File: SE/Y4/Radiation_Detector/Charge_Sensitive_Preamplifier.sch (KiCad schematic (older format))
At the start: 7 parts, among them U1 OP179GRT

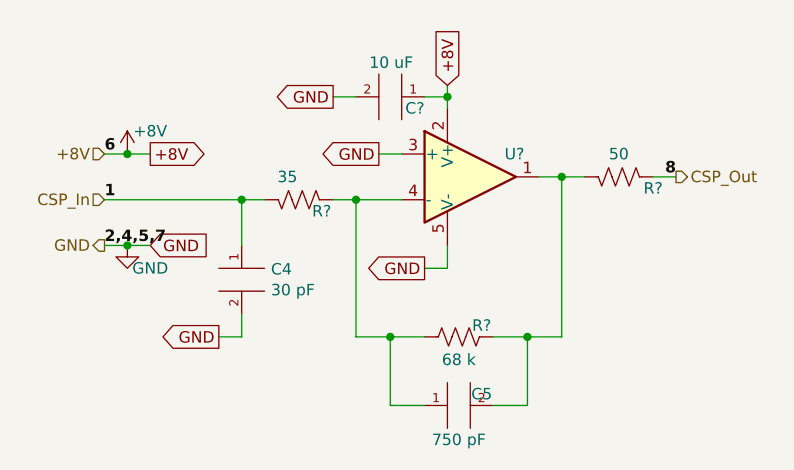
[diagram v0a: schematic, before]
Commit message: SiPM schematic symbol modified
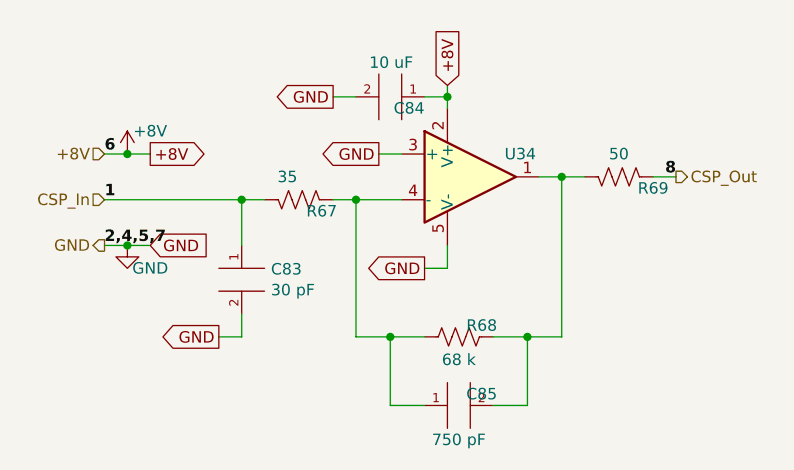
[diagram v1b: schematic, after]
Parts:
- gave numbers to parts that had none: 1
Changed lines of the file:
@@
 $Descr A4 11693 8268
 encoding utf-8
-Sheet 17 33
+Sheet 3 33
 Title ""
 Date ""
@@
 AR Path="/5EC116B0/5EBD2C07/5ED82FF2" Ref="#PWR061"  Part="1"
 AR Path="/5EC11F15/5EBD2C07/5ED82FF2" Ref="#PWR089"  Part="1"
-AR Path="/5EEC0C1C/5EBD2C07/5ED82FF2" Ref="#PWR?"  Part="1"
-AR Path="/5EEC180C/5EBD2C07/5ED82FF2" Ref="#PWR?"  Part="1"
-AR Path="/5EEC25A3/5EBD2C07/5ED82FF2" Ref="#PWR?"  Part="1"
-F 0 "#PWR?" H 1100 1900 50  0001 C CNN
+AR Path="/5EEC0C1C/5EBD2C07/5ED82FF2" Ref="#PWR0124"  Part="1"
+AR Path="/5EEC180C/5EBD2C07/5ED82FF2" Ref="#PWR0131"  Part="1"
+AR Path="/5EEC25A3/5EBD2C07/5ED82FF2" Ref="#PWR0138"  Part="1"
+F 0 "#PWR0138" H 1100 1900 50  0001 C CNN
 F 1 "+8V" H 1200 2150 50  0000 C CNN
 F 2 "" H 1100 2050 50  0001 C CNN
@@
 AR Path="/5EC116B0/5EBD2C07/5ED8301D" Ref="#PWR062"  Part="1"
 AR Path="/5EC11F15/5EBD2C07/5ED8301D" Ref="#PWR090"  Part="1"
-AR Path="/5EEC0C1C/5EBD2C07/5ED8301D" Ref="#PWR?"  Part="1"
-AR Path="/5EEC180C/5EBD2C07/5ED8301D" Ref="#PWR?"  Part="1"
-AR Path="/5EEC25A3/5EBD2C07/5ED8301D" Ref="#PWR?"  Part="1"
-F 0 "#PWR?" H 1100 2200 50  0001 C CNN
+AR Path="/5EEC0C1C/5EBD2C07/5ED8301D" Ref="#PWR0125"  Part="1"
+AR Path="/5EEC180C/5EBD2C07/5ED8301D" Ref="#PWR0132"  Part="1"
+AR Path="/5EEC25A3/5EBD2C07/5ED8301D" Ref="#PWR0139"  Part="1"
+F 0 "#PWR0139" H 1100 2200 50  0001 C CNN
 F 1 "GND" H 1200 2350 50  0000 C CNN
 F 2 "" H 1100 2450 50  0001 C CNN
@@
 AR Path="/5EC116B0/5EBD2C07/5EBE84F9" Ref="R35"  Part="1"
 AR Path="/5EC11F15/5EBD2C07/5EBE84F9" Ref="R48"  Part="1"
-AR Path="/5EEC0C1C/5EBD2C07/5EBE84F9" Ref="R?"  Part="1"
-AR Path="/5EEC180C/5EBD2C07/5EBE84F9" Ref="R?"  Part="1"
-AR Path="/5EEC25A3/5EBD2C07/5EBE84F9" Ref="R?"  Part="1"
-F 0 "R?" V 2500 2950 50  0000 C CNN
+AR Path="/5EEC0C1C/5EBD2C07/5EBE84F9" Ref="R42"  Part="1"
+AR Path="/5EEC180C/5EBD2C07/5EBE84F9" Ref="R55"  Part="1"
+AR Path="/5EEC25A3/5EBD2C07/5EBE84F9" Ref="R68"  Part="1"
+F 0 "R68" V 2500 2950 50  0000 C CNN
 F 1 "68 k" V 2650 2850 50  0000 C CNN
 F 2 "" V 2590 2840 50  0001 C CNN
@@
 AR Path="/5EC116B0/5EBD2C07/5EBE880D" Ref="C31"  Part="1"
 AR Path="/5EC11F15/5EBD2C07/5EBE880D" Ref="C44"  Part="1"
-AR Path="/5EEC0C1C/5EBD2C07/5EBE880D" Ref="C?"  Part="1"
-AR Path="/5EEC180C/5EBD2C07/5EBE880D" Ref="C?"  Part="1"
-AR Path="/5EEC25A3/5EBD2C07/5EBE880D" Ref="C?"  Part="1"
-F 0 "C?" H 2650 3100 50  0000 C CNN
+AR Path="/5EEC0C1C/5EBD2C07/5EBE880D" Ref="C59"  Part="1"
+AR Path="/5EEC180C/5EBD2C07/5EBE880D" Ref="C72"  Part="1"
+AR Path="/5EEC25A3/5EBD2C07/5EBE880D" Ref="C85"  Part="1"
+F 0 "C85" H 2650 3100 50  0000 C CNN
 F 1 "750 pF" H 2550 3300 50  0000 C CNN
 F 2 "" H 2450 3240 50  0001 C CNN
@@
 AR Path="/5EC116B0/5EBD2C07/5EBEB447" Ref="C30"  Part="1"
 AR Path="/5EC11F15/5EBD2C07/5EBEB447" Ref="C43"  Part="1"
-AR Path="/5EEC0C1C/5EBD2C07/5EBEB447" Ref="C?"  Part="1"
-AR Path="/5EEC180C/5EBD2C07/5EBEB447" Ref="C?"  Part="1"
-AR Path="/5EEC25A3/5EBD2C07/5EBEB447" Ref="C?"  Part="1"
-F 0 "C?" V 1704 2578 50  0000 L CNN
+AR Path="/5EEC0C1C/5EBD2C07/5EBEB447" Ref="C57"  Part="1"
+AR Path="/5EEC180C/5EBD2C07/5EBEB447" Ref="C70"  Part="1"
+AR Path="/5EEC25A3/5EBD2C07/5EBEB447" Ref="C83"  Part="1"
+F 0 "C83" V 1704 2578 50  0000 L CNN
 F 1 "30 pF" V 1795 2578 50  0000 L CNN
 F 2 "" H 1650 2540 50  0001 C CNN
@@
 AR Path="/5EC116B0/5EBD2C07/5EBEB46B" Ref="R34"  Part="1"
 AR Path="/5EC11F15/5EBD2C07/5EBEB46B" Ref="R47"  Part="1"
-AR Path="/5EEC0C1C/5EBD2C07/5EBEB46B" Ref="R?"  Part="1"
-AR Path="/5EEC180C/5EBD2C07/5EBEB46B" Ref="R?"  Part="1"
-AR Path="/5EEC25A3/5EBD2C07/5EBEB46B" Ref="R?"  Part="1"
-F 0 "R?" V 1800 2350 50  0000 C CNN
+AR Path="/5EEC0C1C/5EBD2C07/5EBEB46B" Ref="R41"  Part="1"
+AR Path="/5EEC180C/5EBD2C07/5EBEB46B" Ref="R54"  Part="1"
+AR Path="/5EEC25A3/5EBD2C07/5EBEB46B" Ref="R67"  Part="1"
+F 0 "R67" V 1800 2350 50  0000 C CNN
 F 1 "35" V 1950 2200 50  0000 C CNN
 F 2 "" V 1890 2240 50  0001 C CNN
@@
 AR Path="/5EC116B0/5EBD2C07/5EBED0D7" Ref="R36"  Part="1"
 AR Path="/5EC11F15/5EBD2C07/5EBED0D7" Ref="R49"  Part="1"
-AR Path="/5EEC0C1C/5EBD2C07/5EBED0D7" Ref="R?"  Part="1"
-AR Path="/5EEC180C/5EBD2C07/5EBED0D7" Ref="R?"  Part="1"
-AR Path="/5EEC25A3/5EBD2C07/5EBED0D7" Ref="R?"  Part="1"
-F 0 "R?" V 3200 2300 50  0000 C CNN
+AR Path="/5EEC0C1C/5EBD2C07/5EBED0D7" Ref="R43"  Part="1"
+AR Path="/5EEC180C/5EBD2C07/5EBED0D7" Ref="R56"  Part="1"
+AR Path="/5EEC25A3/5EBD2C07/5EBED0D7" Ref="R69"  Part="1"
+F 0 "R69" V 3200 2300 50  0000 C CNN
 F 1 "50" V 3350 2150 50  0000 C CNN
 F 2 "" V 3290 2140 50  0001 C CNN
@@
 AR Path="/5EC116B0/5EBD2C07/5EBE61A1" Ref="U11"  Part="1"
 AR Path="/5EC11F15/5EBD2C07/5EBE61A1" Ref="U16"  Part="1"
-AR Path="/5EEC0C1C/5EBD2C07/5EBE61A1" Ref="U?"  Part="1"
-AR Path="/5EEC180C/5EBD2C07/5EBE61A1" Ref="U?"  Part="1"
-AR Path="/5EEC25A3/5EBD2C07/5EBE61A1" Ref="U?"  Part="1"
-F 0 "U?" H 2750 2250 50  0000 L CNN
+AR Path="/5EEC0C1C/5EBD2C07/5EBE61A1" Ref="U24"  Part="1"
+AR Path="/5EEC180C/5EBD2C07/5EBE61A1" Ref="U29"  Part="1"
+AR Path="/5EEC25A3/5EBD2C07/5EBE61A1" Ref="U34"  Part="1"
+F 0 "U34" H 2750 2250 50  0000 L CNN
 F 1 "OP179GRT" H 2600 2350 50  0001 L CNN
 F 2 "Package_TO_SOT_SMD:SOT-23-5" H 2600 2150 50  0001 C CNN
@@
 	2100 2250 2300 2250
 $Comp
-L 001:C C?
+L 001:C C14
 U 1 1 5EC9647D
 P 2400 1800
-AR Path="/5EBD2B15/5EBD2C07/5EC9647D" Ref="C?"  Part="1"
+AR Path="/5EBD2B15/5EBD2C07/5EC9647D" Ref="C14"  Part="1"
 AR Path="/5EC10E33/5EBD2C07/5EC9647D" Ref="C?"  Part="1"
 AR Path="/5EC116B0/5EBD2C07/5EC9647D" Ref="C?"  Part="1"
 AR Path="/5EC11F15/5EBD2C07/5EC9647D" Ref="C?"  Part="1"
-AR Path="/5EEC0C1C/5EBD2C07/5EC9647D" Ref="C?"  Part="1"
-AR Path="/5EEC180C/5EBD2C07/5EC9647D" Ref="C?"  Part="1"
-AR Path="/5EEC25A3/5EBD2C07/5EC9647D" Ref="C?"  Part="1"
-F 0 "C?" H 2400 1850 50  0000 L CNN
+AR Path="/5EEC0C1C/5EBD2C07/5EC9647D" Ref="C58"  Part="1"
+AR Path="/5EEC180C/5EBD2C07/5EC9647D" Ref="C71"  Part="1"
+AR Path="/5EEC25A3/5EBD2C07/5EC9647D" Ref="C84"  Part="1"
+F 0 "C84" H 2400 1850 50  0000 L CNN
 F 1 "10 uF" H 2450 1650 50  0000 L CNN
 F 2 "" H 2450 1890 50  0001 C CNN

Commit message: cleaned up schematic and clarified
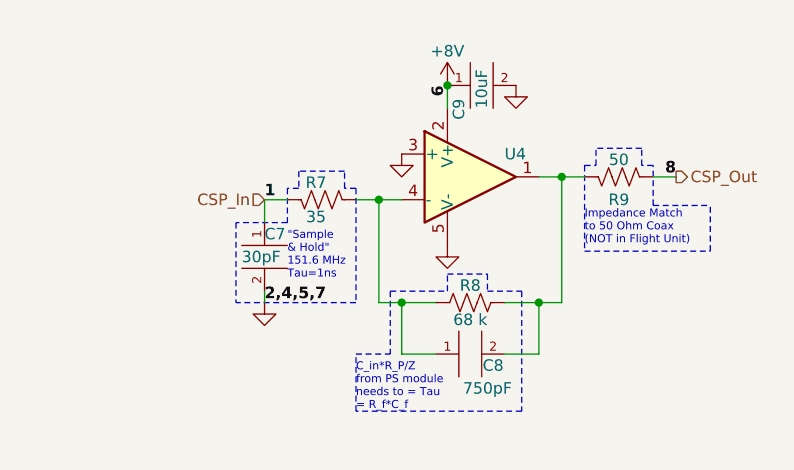
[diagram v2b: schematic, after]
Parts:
- C7: renamed from C4; value 30 pF -> 30pF
- C8: renamed from C5; value 750 pF -> 750pF
- C9: renamed from C14; value 10 uF -> 10uF
- renumbered R8 to R7, R9 to R8, R10 to R9, U1 to U4
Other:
- note added: ""Sample\n& Hold"\n151.6 MHz\nTau=1ns"
- note added: "C_in*R_P/Z\nfrom PS module\nneeds to = Tau\n= R_f*C_f"
- note added: "Impedance Match\nto 50 Ohm Coax\n(NOT in Flight Unit)"
- moved on the sheet: C7, C8, C9, R7, R8

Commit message: updated schematic labeling
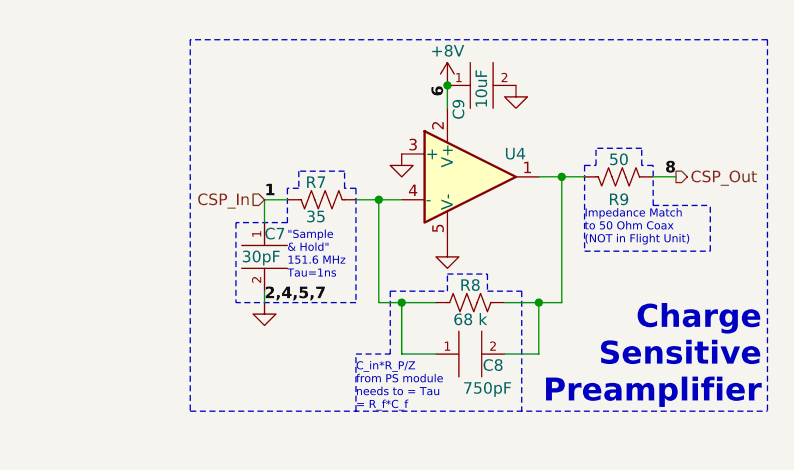
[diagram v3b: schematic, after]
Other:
- note added: "Charge\nSensitive\nPreamplifier"
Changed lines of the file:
@@
 AR Path="/5EE9A91A/5EBD2C07/5ED82FF2" Ref="#PWR0101"  Part="1"
 AR Path="/5EE9D7FB/5EBD2C07/5ED82FF2" Ref="#PWR0128"  Part="1"
+AR Path="/5EBD2B15/5ECB2930/5ED82FF2" Ref="#PWR?"  Part="1"
+AR Path="/5EE979F5/5ECB2930/5ED82FF2" Ref="#PWR?"  Part="1"
+AR Path="/5EE9A91A/5ECB2930/5ED82FF2" Ref="#PWR?"  Part="1"
+AR Path="/5EE9D7FB/5ECB2930/5ED82FF2" Ref="#PWR?"  Part="1"
 F 0 "#PWR022" H 2500 1600 50  0001 C CNN
 F 1 "+8V" H 2500 1900 50  0000 C CNN
@@
 AR Path="/5EE9A91A/5EBD2C07/5EBE84F9" Ref="R54"  Part="1"
 AR Path="/5EE9D7FB/5EBD2C07/5EBE84F9" Ref="R67"  Part="1"
+AR Path="/5EBD2B15/5ECB2930/5EBE84F9" Ref="R?"  Part="1"
+AR Path="/5EE979F5/5ECB2930/5EBE84F9" Ref="R?"  Part="1"
+AR Path="/5EE9A91A/5ECB2930/5EBE84F9" Ref="R?"  Part="1"
+AR Path="/5EE9D7FB/5ECB2930/5EBE84F9" Ref="R?"  Part="1"
 F 0 "R8" V 2525 2700 50  0000 C CNN
 F 1 "68 k" V 2675 2700 50  0000 C CNN
@@
 AR Path="/5EE9A91A/5EBD2C07/5EBE880D" Ref="C71"  Part="1"
 AR Path="/5EE9D7FB/5EBD2C07/5EBE880D" Ref="C84"  Part="1"
+AR Path="/5EBD2B15/5ECB2930/5EBE880D" Ref="C?"  Part="1"
+AR Path="/5EE979F5/5ECB2930/5EBE880D" Ref="C?"  Part="1"
+AR Path="/5EE9A91A/5ECB2930/5EBE880D" Ref="C?"  Part="1"
+AR Path="/5EE9D7FB/5ECB2930/5EBE880D" Ref="C?"  Part="1"
 F 0 "C8" H 2700 2975 50  0000 C CNN
 F 1 "750pF" H 2675 3075 50  0000 C CNN
@@
 AR Path="/5EE9A91A/5EBD2C07/5EBEB447" Ref="C70"  Part="1"
 AR Path="/5EE9D7FB/5EBD2C07/5EBEB447" Ref="C83"  Part="1"
+AR Path="/5EBD2B15/5ECB2930/5EBEB447" Ref="C?"  Part="1"
+AR Path="/5EE979F5/5ECB2930/5EBEB447" Ref="C?"  Part="1"
+AR Path="/5EE9A91A/5ECB2930/5EBEB447" Ref="C?"  Part="1"
+AR Path="/5EE9D7FB/5ECB2930/5EBEB447" Ref="C?"  Part="1"
 F 0 "C7" V 1750 2350 50  0000 L CNN
 F 1 "30pF" V 1850 2250 50  0000 L CNN
@@
 AR Path="/5EE9A91A/5EBD2C07/5EBEB46B" Ref="R53"  Part="1"
 AR Path="/5EE9D7FB/5EBD2C07/5EBEB46B" Ref="R66"  Part="1"
+AR Path="/5EBD2B15/5ECB2930/5EBEB46B" Ref="R?"  Part="1"
+AR Path="/5EE979F5/5ECB2930/5EBEB46B" Ref="R?"  Part="1"
+AR Path="/5EE9A91A/5ECB2930/5EBEB46B" Ref="R?"  Part="1"
+AR Path="/5EE9D7FB/5ECB2930/5EBEB46B" Ref="R?"  Part="1"
 F 0 "R7" V 2025 2225 50  0000 C CNN
 F 1 "35" V 1875 2225 50  0000 C CNN
@@
 AR Path="/5EE9A91A/5EBD2C07/5EBED0D7" Ref="R55"  Part="1"
 AR Path="/5EE9D7FB/5EBD2C07/5EBED0D7" Ref="R68"  Part="1"
+AR Path="/5EBD2B15/5ECB2930/5EBED0D7" Ref="R?"  Part="1"
+AR Path="/5EE979F5/5ECB2930/5EBED0D7" Ref="R?"  Part="1"
+AR Path="/5EE9A91A/5ECB2930/5EBED0D7" Ref="R?"  Part="1"
+AR Path="/5EE9D7FB/5ECB2930/5EBED0D7" Ref="R?"  Part="1"
 F 0 "R9" V 3150 2150 50  0000 C CNN
 F 1 "50" V 3325 2150 50  0000 C CNN
@@
 AR Path="/5EE9A91A/5EBD2C07/5EBE61A1" Ref="U29"  Part="1"
 AR Path="/5EE9D7FB/5EBD2C07/5EBE61A1" Ref="U34"  Part="1"
+AR Path="/5EBD2B15/5ECB2930/5EBE61A1" Ref="U?"  Part="1"
+AR Path="/5EE979F5/5ECB2930/5EBE61A1" Ref="U?"  Part="1"
+AR Path="/5EE9A91A/5ECB2930/5EBE61A1" Ref="U?"  Part="1"
+AR Path="/5EE9D7FB/5ECB2930/5EBE61A1" Ref="U?"  Part="1"
 F 0 "U4" H 2750 2250 50  0000 L CNN
 F 1 "OP179GRT" H 2600 2350 50  0001 L CNN
@@
 AR Path="/5EE9A91A/5EBD2C07/5ED8BAA5" Ref="#PWR0100"  Part="1"
 AR Path="/5EE9D7FB/5EBD2C07/5ED8BAA5" Ref="#PWR0127"  Part="1"
+AR Path="/5EBD2B15/5ECB2930/5ED8BAA5" Ref="#PWR?"  Part="1"
+AR Path="/5EE979F5/5ECB2930/5ED8BAA5" Ref="#PWR?"  Part="1"
+AR Path="/5EE9A91A/5ECB2930/5ED8BAA5" Ref="#PWR?"  Part="1"
+AR Path="/5EE9D7FB/5ECB2930/5ED8BAA5" Ref="#PWR?"  Part="1"
 F 0 "#PWR021" H 2300 1800 50  0001 C CNN
 F 1 "GND" H 2200 2050 50  0001 C CNN
@@
 AR Path="/5EE9A91A/5EBD2C07/5ED8BB73" Ref="#PWR099"  Part="1"
 AR Path="/5EE9D7FB/5EBD2C07/5ED8BB73" Ref="#PWR0126"  Part="1"
+AR Path="/5EBD2B15/5ECB2930/5ED8BB73" Ref="#PWR?"  Part="1"
+AR Path="/5EE979F5/5ECB2930/5ED8BB73" Ref="#PWR?"  Part="1"
+AR Path="/5EE9A91A/5ECB2930/5ED8BB73" Ref="#PWR?"  Part="1"
+AR Path="/5EE9D7FB/5ECB2930/5ED8BB73" Ref="#PWR?"  Part="1"
 F 0 "#PWR020" H 1700 2450 50  0001 C CNN
 F 1 "GND" H 1600 2700 50  0001 C CNN
@@
 AR Path="/5EE9A91A/5EBD2C07/5ED8CC65" Ref="#PWR0102"  Part="1"
 AR Path="/5EE9D7FB/5EBD2C07/5ED8CC65" Ref="#PWR0129"  Part="1"
+AR Path="/5EBD2B15/5ECB2930/5ED8CC65" Ref="#PWR?"  Part="1"
+AR Path="/5EE979F5/5ECB2930/5ED8CC65" Ref="#PWR?"  Part="1"
+AR Path="/5EE9A91A/5ECB2930/5ED8CC65" Ref="#PWR?"  Part="1"
+AR Path="/5EE9D7FB/5ECB2930/5ED8CC65" Ref="#PWR?"  Part="1"
 F 0 "#PWR023" H 2500 2200 50  0001 C CNN
 F 1 "GND" H 2400 2450 50  0001 C CNN
@@
 AR Path="/5EE9A91A/5EBD2C07/5ED8DA9C" Ref="#PWR0103"  Part="1"
 AR Path="/5EE9D7FB/5EBD2C07/5ED8DA9C" Ref="#PWR0130"  Part="1"
+AR Path="/5EBD2B15/5ECB2930/5ED8DA9C" Ref="#PWR?"  Part="1"
+AR Path="/5EE979F5/5ECB2930/5ED8DA9C" Ref="#PWR?"  Part="1"
+AR Path="/5EE9A91A/5ECB2930/5ED8DA9C" Ref="#PWR?"  Part="1"
+AR Path="/5EE9D7FB/5ECB2930/5ED8DA9C" Ref="#PWR?"  Part="1"
 F 0 "#PWR024" H 2800 1500 50  0001 C CNN
 F 1 "GND" H 2700 1750 50  0001 C CNN
@@
 AR Path="/5EE9A91A/5EBD2C07/5EC9647D" Ref="C72"  Part="1"
 AR Path="/5EE9D7FB/5EBD2C07/5EC9647D" Ref="C85"  Part="1"
+AR Path="/5EBD2B15/5ECB2930/5EC9647D" Ref="C?"  Part="1"
+AR Path="/5EE979F5/5ECB2930/5EC9647D" Ref="C?"  Part="1"
+AR Path="/5EE9A91A/5ECB2930/5EC9647D" Ref="C?"  Part="1"
+AR Path="/5EE9D7FB/5ECB2930/5EC9647D" Ref="C?"  Part="1"
 F 0 "C9" V 2550 1600 50  0000 L CNN
 F 1 "10uF" V 2650 1650 50  0000 L CNN
@@
 	2250 2650 2500 2650
 Wire Notes Line
-	2825 3175 2100 3175
-Wire Notes Line
 	2100 2700 1575 2700
 Wire Notes Line
@@
 Wire Wire Line
 	1700 2650 1700 2700
+Text Notes 3875 3150 2    100  ~ 20
+Charge\nSensitive\nPreamplifier
+Wire Notes Line
+	3900 1550 1375 1550
+Wire Notes Line
+	1375 1550 1375 3175
+Wire Notes Line
+	3900 1550 3900 3175
+Wire Notes Line
+	1375 3175 3900 3175
 $EndSCHEMATC
